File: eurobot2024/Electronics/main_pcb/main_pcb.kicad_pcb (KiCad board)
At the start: 2 copper layers, 77.5 x 89 mm, 58 parts, among them J1 PI40HAT, J10 Conn_01x02_Male, J11 Conn_01x03_Male, J12 Conn_01x02_Male, J13 Conn_01x02_Male, J14 Conn_01x04_Male, J15 Conn_01x02_Male, J16 Conn_01x02_Male, J17 Conn_01x03_Male, J18 Conn_01x03_Male, J19 Conn_01x04_Male, J2 Conn_01x02_Male, J20 Conn_01x05, J21 Conn_01x05, J22 Conn_01x05, J23 22-03-5035, J24 Conn_01x02_Male, J3 Conn_01x02_Male, J4 Conn_01x02_Male, J5 Conn_01x02_Male, J6 Conn_01x02_Male, J7 Conn_01x04_Male, J8 Conn_01x02_Male, J9 22-03-5035, P1 R-78Bxx-2.0, P2 Amazon 10A stepdown, Q1 NVTR4503NT1G, Q2 NVTR4503NT1G, Q3 NVTR4503NT1G, Q7 NVTR4503NT1G, U1 74LVC1G125, U2 SN74LVC1G04DRLR, U3 PCA9306D, U4 Pololu_MAX14870, U5 PCA9685PW, U6 Pololu_MAX14870, U7 SN74AHCT1G126

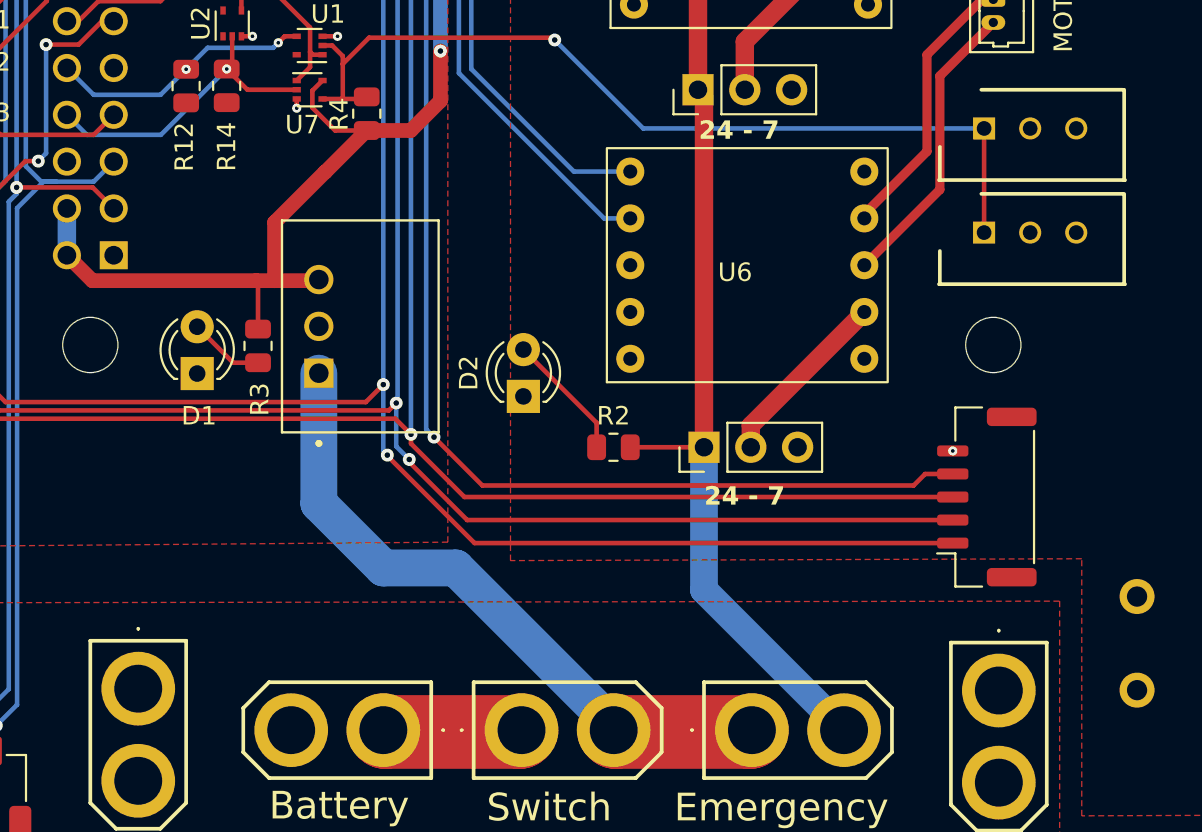
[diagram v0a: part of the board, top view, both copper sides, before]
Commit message: Rename SPI1 to SPI0 & add some text
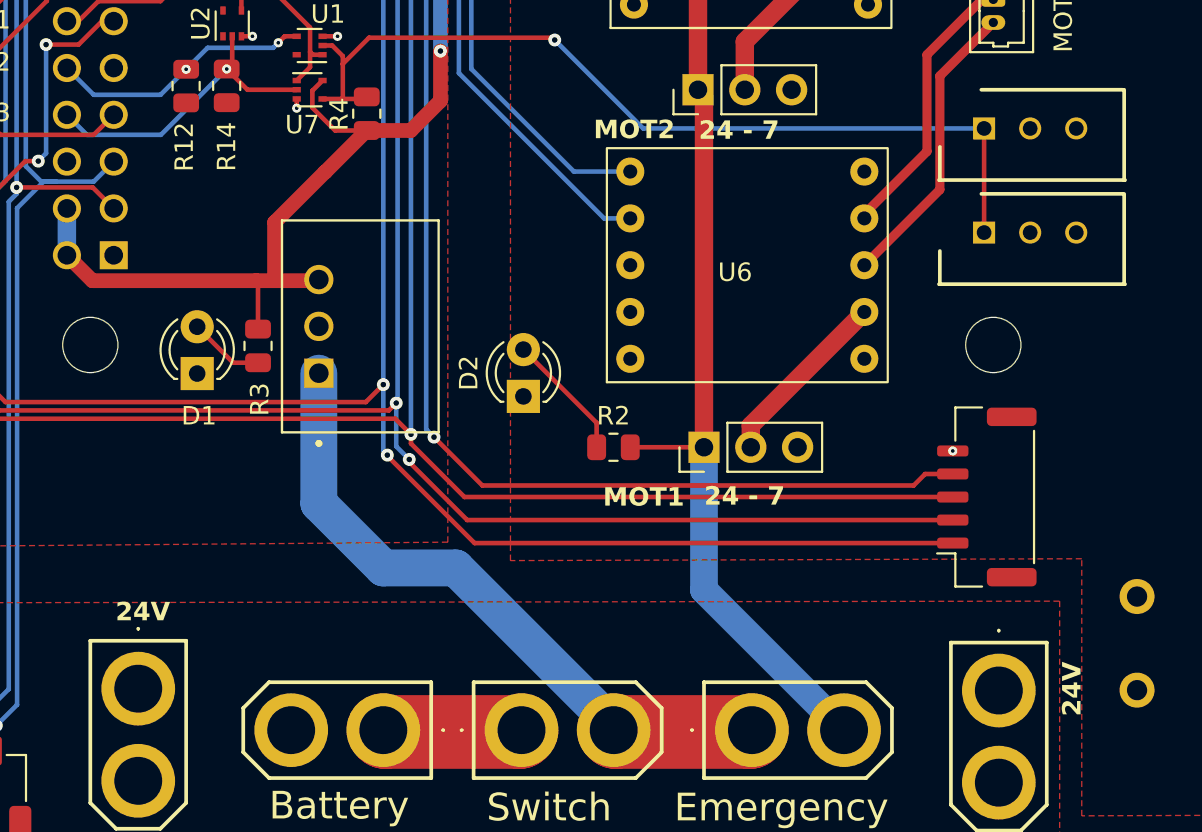
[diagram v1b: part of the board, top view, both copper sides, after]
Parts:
- renumbered SPI1 to SPI0
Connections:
- net /SPI1 CLK renamed /SPI0 CLK
- net /SPI1 MISO renamed /SPI0 MISO
- net /SPI1 MOSI renamed /SPI0 MOSI
- net /SPI1_CS0 renamed /SPI0_CS0
- net /SPI1_CS1 renamed /SPI0_CS1
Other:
- board text added: "24V"

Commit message: Main robot PCB order
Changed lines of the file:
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@@
     (effects (font (size 1 1) (thickness 0.2) bold))
   )
-  (gr_text "24V" (at 138.768 137.668 90) (layer "F.SilkS")
+  (gr_text "24V" (at 134.75 133.75) (layer "F.SilkS")
     (effects (font (size 1 1) (thickness 0.2) bold))
   )
@@
       (pts
         (xy 138.1 132.9)
-        (xy 138.1 149.5)
-        (xy 69.12 149.125)
+        (xy 138.1 147)
+        (xy 69.5 147)
         (xy 69 133)
       )
@@
     (polygon
       (pts
-        (xy 152.5 144.5)
+        (xy 147 144.5)
         (xy 139.3 144.55)
         (xy 139.3 130.6)
@@
         (xy 108.3 67.6)
         (xy 96.1 67.6)
-        (xy 96.1 55.85)
-        (xy 153.1 55.75)
+        (xy 96.1 58)
+        (xy 147 58)
       )
     )
@@
     (polygon
       (pts
-        (xy 150.345 149.725)
-        (xy 66.6 149)
-        (xy 66.6 56.7)
-        (xy 150.345 57.2436)
+        (xy 147 147)
+        (xy 69.5 147)
+        (xy 69.5 58)
+        (xy 147 58)
       )
     )

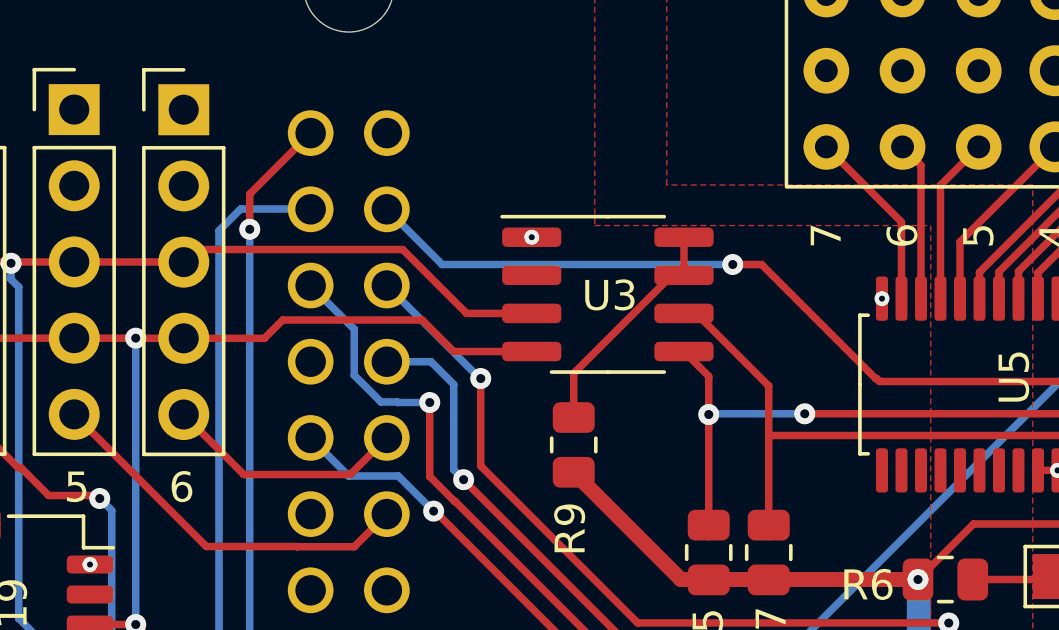
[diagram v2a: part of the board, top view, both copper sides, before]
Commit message: Implement fully action-based strategy framework for 2024 robot.
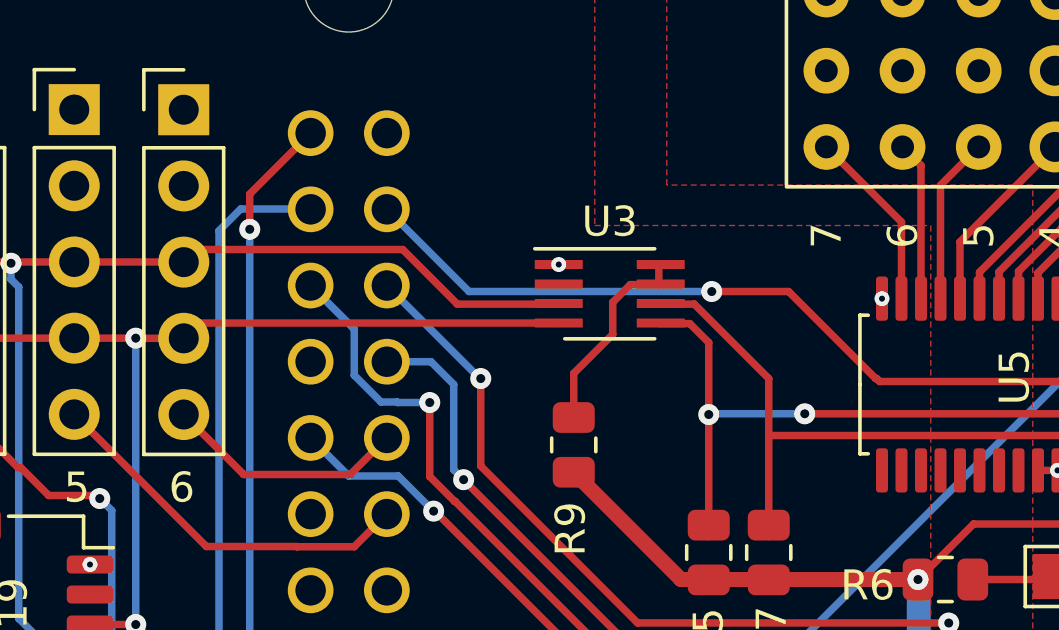
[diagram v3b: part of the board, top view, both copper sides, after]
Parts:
- U3: footprint Package_SO:SOP-8_3.76x4.96mm_P1.27mm -> Package_SO:SSOP-8_2.95x2.8mm_P0.65mm
- moved U3 0.07 mm to (94.2, 71.2)
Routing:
- net Net-(U3-SDA2): track 21.3 -> 23.2 mm
- net Net-(U3-SCL2): track 20.3 -> 21.8 mm
- net /I2C SCL: track 104.0 -> 104.7 mm
- net Net-(U3-EN): track 7.36 -> 6.81 mm

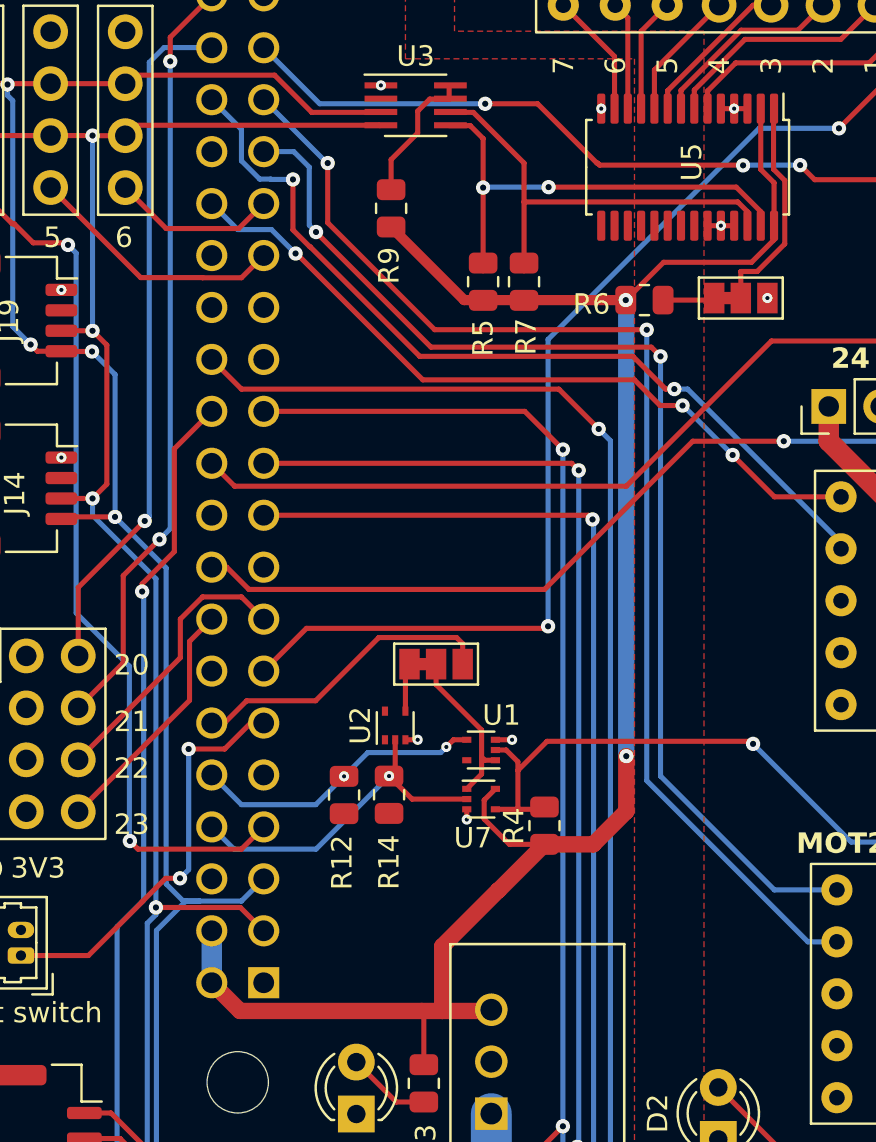
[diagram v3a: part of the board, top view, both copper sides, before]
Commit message: [main_pcb] Update component footprint for easier soldering
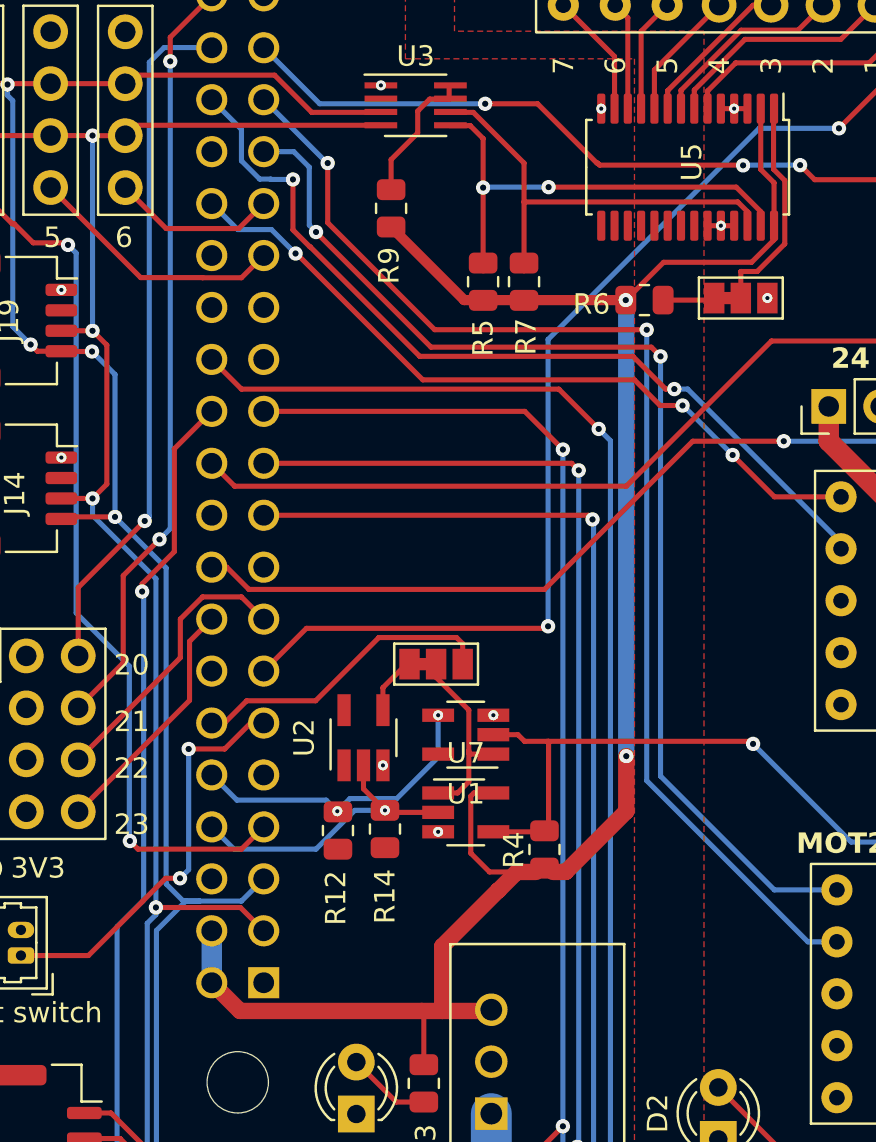
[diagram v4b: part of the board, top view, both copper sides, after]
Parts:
- U1: value 74LVC1G125 -> SN74LVC1G125DBVR; footprint Package_TO_SOT_SMD:SOT-553 -> Package_TO_SOT_SMD:SOT-23-5_HandSoldering
- U2: value SN74LVC1G04DRLR -> SN74LVC1G04DBVR; footprint Package_TO_SOT_SMD:SOT-553 -> Package_TO_SOT_SMD:SOT-23-5_HandSoldering
- U7: value SN74AHCT1G126 -> SN74AHCT1G126DBVR; footprint Package_TO_SOT_SMD:SOT-553 -> Package_TO_SOT_SMD:SOT-23-5_HandSoldering
- moved R12 1.76 mm to (90.4, 106.7)
- moved R14 1.69 mm to (92.7, 106.6)
- moved U2 1.66 mm to (91.7, 102.2)
- moved R4 1.16 mm to (100.5, 107.6)
- moved U1 1.06 mm to (96.7, 102.0)
- moved U7 0.99 mm to (96.7, 105.8)
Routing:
- net GND: track 4.48 -> 2.56 mm
- net /UART_HalfDuplex: track 48.9 -> 50.5 mm
- net /UART_TX: track 16.3 -> 14.8 mm
- net +5V: track 92.5 -> 94.0 mm
- net /TX_EN: track 8.06 -> 9.36 mm
- net /I2C SDA: track 99.8 -> 99.1 mm
- net /UART_RX: track 14.4 -> 14.9 mm
